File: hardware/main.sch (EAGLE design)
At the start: 96 parts, among them IC1 IS61WV102416BLL-10T, U1 LCMXO2-7000HC-4TG144I, U3 W25Q32FV

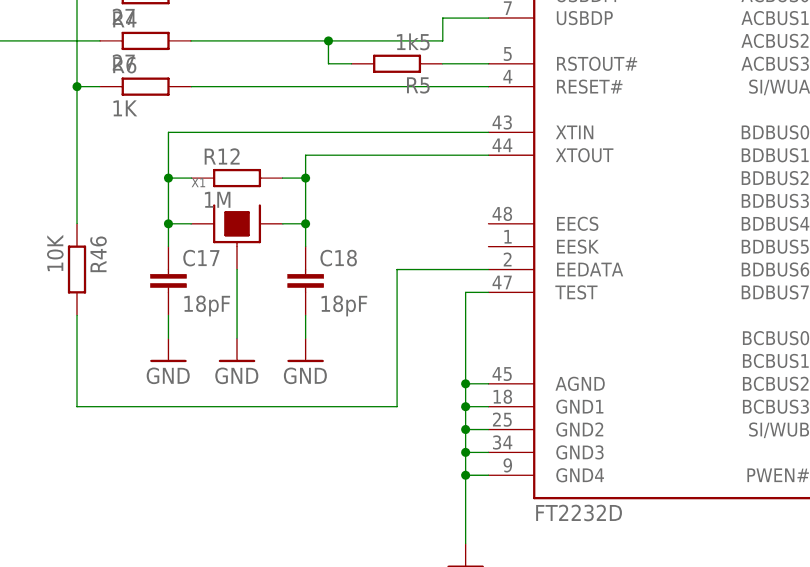
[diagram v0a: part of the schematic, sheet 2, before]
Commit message: 6MHz TSX3225 replaced with 6x3
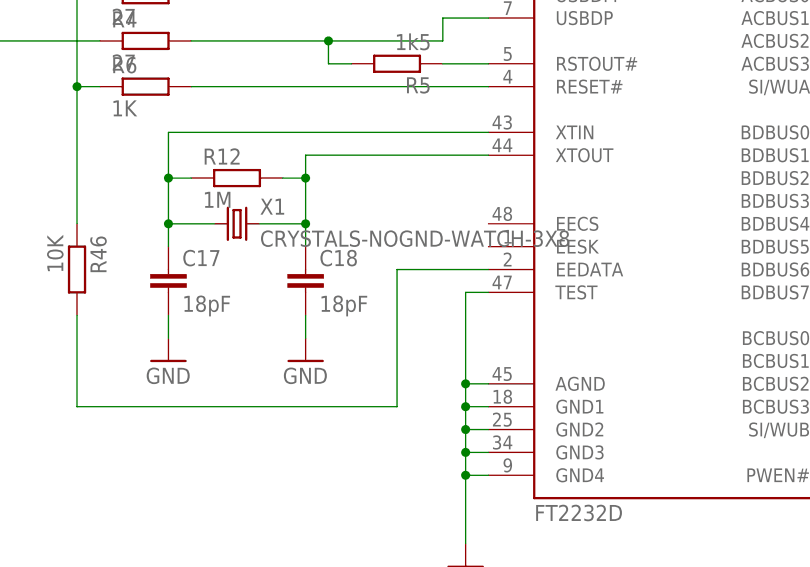
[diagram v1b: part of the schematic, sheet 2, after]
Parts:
- X1: value (none) -> CRYSTALS-NOGND-WATCH-3X8; device PP_FreqCtrl:SHIELDED_CRYSTAL_TSX-3225 -> IQD-Frequency-Products:CRYSTALS-NOGND-WATCH-3X8
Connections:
- net GND: no longer X1.P$3
- net N$17: now also X1.1; no longer X1.P$1
- net N$18: now also X1.2; no longer X1.P$2
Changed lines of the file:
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@@
 <part name="U$12" library="mouse_enc" deviceset="SWITCH_6X6" device=""/>
 <part name="GND17" library="supply1" library_urn="urn:adsk.eagle:library:371" deviceset="GND" device=""/>
-<part name="X1" library="PP_FreqCtrl" deviceset="SHIELDED_CRYSTAL" device="_TSX-3225"/>
-<part name="GND20" library="supply1" library_urn="urn:adsk.eagle:library:371" deviceset="GND" device=""/>
 <part name="Q1" library="crystal-geyer_V1_0" library_urn="urn:adsk.eagle:library:203" deviceset="KXO-TCXO-CMOS" device="-82" package3d_urn="urn:adsk.eagle:package:11956/1"/>
 <part name="R11" library="resistor" library_urn="urn:adsk.eagle:library:348" deviceset="R-EU_" device="R0603" package3d_urn="urn:adsk.eagle:package:26057/1" value="10"/>
@@
 <part name="GND31" library="supply1" library_urn="urn:adsk.eagle:library:371" deviceset="GND" device=""/>
 <part name="+3V20" library="supply1" library_urn="urn:adsk.eagle:library:371" deviceset="+3V3" device=""/>
+<part name="X1" library="IQD-Frequency-Products" library_urn="urn:adsk.eagle:library:90" deviceset="CRYSTALS-NOGND" device="-WATCH-3X8" package3d_urn="urn:adsk.eagle:package:3354/1"/>
 </parts>
 <sheets>
@@
 <instance part="P+1" gate="1" x="12.7" y="53.34"/>
 <instance part="P+2" gate="1" x="50.8" y="198.12"/>
-<instance part="X1" gate="G$1" x="68.58" y="129.54"/>
-<instance part="GND20" gate="1" x="68.58" y="114.3"/>
 <instance part="JP1" gate="A" x="119.38" y="50.8"/>
 <instance part="GND23" gate="1" x="106.68" y="33.02"/>
@@
 <instance part="LED2" gate="G$1" x="45.72" y="30.48" rot="MR0"/>
 <instance part="R47" gate="G$1" x="45.72" y="40.64" rot="R270"/>
+<instance part="X1" gate="G$1" x="68.58" y="129.54"/>
 </instances>
 <busses>
@@
 </segment>
 <segment>
-<pinref part="X1" gate="G$1" pin="P$3"/>
-<pinref part="GND20" gate="1" pin="GND"/>
-<wire x1="68.58" y1="124.46" x2="68.58" y2="116.84" width="0.1524" layer="91"/>
-</segment>
-<segment>
 <pinref part="JP1" gate="A" pin="11"/>
 <pinref part="GND23" gate="1" pin="GND"/>
@@
 <wire x1="60.96" y1="134.62" x2="63.5" y2="134.62" width="0.1524" layer="91"/>
 <junction x="60.96" y="134.62"/>
-<pinref part="X1" gate="G$1" pin="P$1"/>
-<wire x1="60.96" y1="129.54" x2="63.5" y2="129.54" width="0.1524" layer="91"/>
 <junction x="60.96" y="129.54"/>
+<pinref part="X1" gate="G$1" pin="1"/>
+<wire x1="60.96" y1="129.54" x2="66.04" y2="129.54" width="0.1524" layer="91"/>
 </segment>
 </net>
@@
 <wire x1="76.2" y1="137.16" x2="96.52" y2="137.16" width="0.1524" layer="91"/>
 <junction x="76.2" y="134.62"/>
-<pinref part="X1" gate="G$1" pin="P$2"/>
-<wire x1="73.66" y1="129.54" x2="76.2" y2="129.54" width="0.1524" layer="91"/>
 <junction x="76.2" y="129.54"/>
-</segment>
-</net>
+<pinref part="X1" gate="G$1" pin="2"/>
+<wire x1="76.2" y1="129.54" x2="71.12" y2="129.54" width="0.1524" layer="91"/>
+</segment>
+</net>

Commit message: schematic fixes
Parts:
- C17, C18: value 18pF -> 27pF
- R12: value 1M -> DNP
- R47: value 470 -> 1K
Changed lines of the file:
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@@
 <part name="C15" library="resistor" library_urn="urn:adsk.eagle:library:348" deviceset="C-EU" device="C0603" package3d_urn="urn:adsk.eagle:package:26138/1" value="100nF"/>
 <part name="GND15" library="supply1" library_urn="urn:adsk.eagle:library:371" deviceset="GND" device=""/>
-<part name="R12" library="resistor" library_urn="urn:adsk.eagle:library:348" deviceset="R-EU_" device="R0603" package3d_urn="urn:adsk.eagle:package:26057/1" value="1M"/>
-<part name="C17" library="resistor" library_urn="urn:adsk.eagle:library:348" deviceset="C-EU" device="C0603" package3d_urn="urn:adsk.eagle:package:26138/1" value="18pF"/>
-<part name="C18" library="resistor" library_urn="urn:adsk.eagle:library:348" deviceset="C-EU" device="C0603" package3d_urn="urn:adsk.eagle:package:26138/1" value="18pF"/>
+<part name="R12" library="resistor" library_urn="urn:adsk.eagle:library:348" deviceset="R-EU_" device="R0603" package3d_urn="urn:adsk.eagle:package:26057/1" value="DNP"/>
+<part name="C17" library="resistor" library_urn="urn:adsk.eagle:library:348" deviceset="C-EU" device="C0603" package3d_urn="urn:adsk.eagle:package:26138/1" value="27pF"/>
+<part name="C18" library="resistor" library_urn="urn:adsk.eagle:library:348" deviceset="C-EU" device="C0603" package3d_urn="urn:adsk.eagle:package:26138/1" value="27pF"/>
 <part name="GND18" library="supply1" library_urn="urn:adsk.eagle:library:371" deviceset="GND" device=""/>
 <part name="GND19" library="supply1" library_urn="urn:adsk.eagle:library:371" deviceset="GND" device=""/>
@@
 <part name="R46" library="resistor" library_urn="urn:adsk.eagle:library:348" deviceset="R-EU_" device="R0603" package3d_urn="urn:adsk.eagle:package:26057/1" value="10K"/>
 <part name="LED2" library="led" library_urn="urn:adsk.eagle:library:259" deviceset="LED" device="CHIPLED_0603" package3d_urn="urn:adsk.eagle:package:15822/2"/>
-<part name="R47" library="resistor" library_urn="urn:adsk.eagle:library:348" deviceset="R-EU_" device="R0603" package3d_urn="urn:adsk.eagle:package:26057/1" value="470"/>
+<part name="R47" library="resistor" library_urn="urn:adsk.eagle:library:348" deviceset="R-EU_" device="R0603" package3d_urn="urn:adsk.eagle:package:26057/1" value="1K"/>
 <part name="C26" library="resistor" library_urn="urn:adsk.eagle:library:348" deviceset="C-EU" device="C0603" package3d_urn="urn:adsk.eagle:package:26138/1" value="100nF"/>
 <part name="C27" library="resistor" library_urn="urn:adsk.eagle:library:348" deviceset="C-EU" device="C0603" package3d_urn="urn:adsk.eagle:package:26138/1" value="100nF"/>

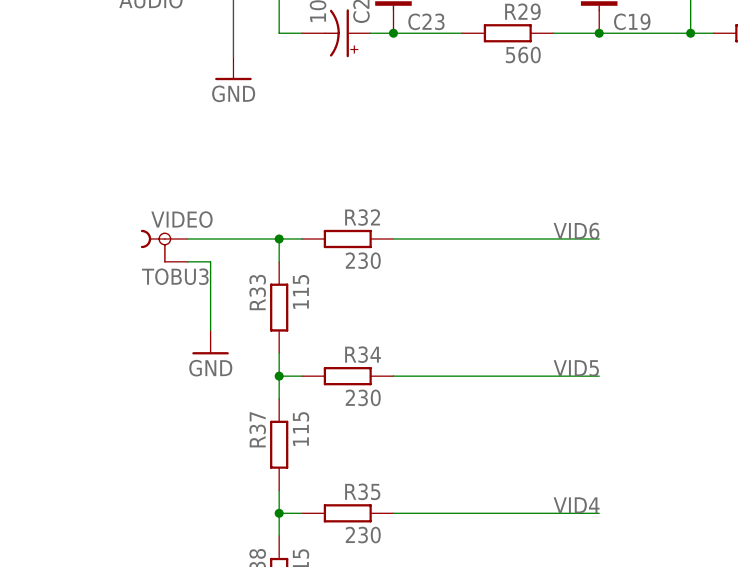
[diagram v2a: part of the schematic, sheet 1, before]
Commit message: 6-bit video dac
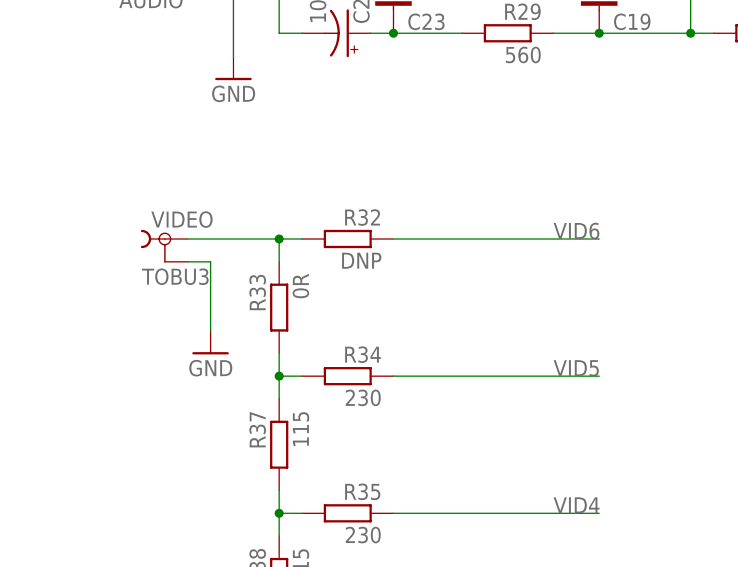
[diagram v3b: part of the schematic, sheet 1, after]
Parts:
- R32: value 230 -> DNP
- R33: value 115 -> 0R
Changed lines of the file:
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@@
 <part name="C25" library="SparkFun" deviceset="CAP_POL" device="7343" value="100uF"/>
 <part name="GND27" library="supply1" library_urn="urn:adsk.eagle:library:371" deviceset="GND" device=""/>
-<part name="R32" library="resistor" library_urn="urn:adsk.eagle:library:348" deviceset="R-EU_" device="R0603" package3d_urn="urn:adsk.eagle:package:26057/1" value="230"/>
-<part name="R33" library="resistor" library_urn="urn:adsk.eagle:library:348" deviceset="R-EU_" device="R0603" package3d_urn="urn:adsk.eagle:package:26057/1" value="115"/>
+<part name="R32" library="resistor" library_urn="urn:adsk.eagle:library:348" deviceset="R-EU_" device="R0603" package3d_urn="urn:adsk.eagle:package:26057/1" value="DNP"/>
+<part name="R33" library="resistor" library_urn="urn:adsk.eagle:library:348" deviceset="R-EU_" device="R0603" package3d_urn="urn:adsk.eagle:package:26057/1" value="0R"/>
 <part name="R34" library="resistor" library_urn="urn:adsk.eagle:library:348" deviceset="R-EU_" device="R0603" package3d_urn="urn:adsk.eagle:package:26057/1" value="230"/>
 <part name="R35" library="resistor" library_urn="urn:adsk.eagle:library:348" deviceset="R-EU_" device="R0603" package3d_urn="urn:adsk.eagle:package:26057/1" value="230"/>

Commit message: Schematic and pcb fixes. Removed vid6 from video dac, io0 from GPIO port. Missed keyboard lines connected: ps2data to vid6, ps2clk to io0
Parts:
- removed R32: DNP, resistor:R-EU_R0603
- removed R33: 0R, resistor:R-EU_R0603
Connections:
- removed net IO0: JP3.1, U1A.PL3B
- removed net N$21: R32.2, R33.1, VIDEO.1
- removed net VID6: R32.1, U1B.PT11B
- net GND: now also JP3.1
- net N$25: now also VIDEO.1; no longer R33.2
- net PS2_CLOCK: now also U1A.PL3B
- net PS2_DATA: now also U1B.PT11B
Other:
- moved on the sheet: R34, R35, R36, R37, R38, R39, R40, R41, R42, R43, R44, R45
